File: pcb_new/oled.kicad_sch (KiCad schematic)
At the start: 33 parts, among them J10 3-2328724-1, U8 TPS6734ID

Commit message: initial test of new board
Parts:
- removed D1: SS12, OroLink:DIOM5027X244N, symbol OroLink:SS12
- added D1: SS12, OroLink:DIOM5027X244N, symbol SamacSys_Parts:SS12
- C105, C114, C115, C148: Mouser Part Number 81-GRM15C61E475ME15J -> (none)
- C89, C97: Mouser Part Number (none) -> 74-293D336X0020D2TE3; Mouser Price/Stock (none) -> https://www.mouser.de/ProductDetail/Vishay-Sprague/293D336X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
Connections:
- net +12V: now also D1.1
- net at L1.2, U8.6 (OUT): now also D1.2
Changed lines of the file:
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@@
 	)
 	(junction
-		(at 156.21 104.14)
-		(diameter 0)
-		(color 0 0 0 0)
-	)
-	(junction
 		(at 102.87 78.74)
 		(diameter 0)
@@
 	)
 	(junction
+		(at 156.21 104.14)
+		(diameter 0)
+		(color 0 0 0 0)
+	)
+	(junction
 		(at 243.84 120.65)
 		(diameter 0)
@@
 			)
 		)
-		(property "Mouser Part Number" "81-GRM15C61E475ME15J"
+		(property "Mouser Part Number" ""
 			(at 238.76 746.99 0)
 			(effects
@@
 	)
 	(symbol
-		(lib_id "OroLink:SS12")
-		(at 158.75 104.14 180)
-		(unit 1)
-		(exclude_from_sim no)
-		(in_bom yes)
-		(on_board yes)
-		(dnp no)
-		(fields_autoplaced yes)
-		(property "Reference" "D1"
-			(at 148.59 97.4555 0)
-			(effects
-				(font
-					(size 1.27 1.27)
-				)
-			)
-		)
-		(property "Value" "SS12"
-			(at 148.59 99.8798 0)
-			(effects
-				(font
-					(size 1.27 1.27)
-				)
-			)
-		)
-		(property "Footprint" "OroLink:DIOM5027X244N"
-			(at 146.05 10.49 0)
-			(effects
-				(font
-					(size 1.27 1.27)
-				)
-				(justify left top)
-				(hide yes)
-			)
-		)
-		(property "Datasheet" "https://www.panjit.com.tw/en/Product/downloadPDF/SS12"
-			(at 146.05 -89.51 0)
-			(effects
-				(font
-					(size 1.27 1.27)
-				)
-				(justify left top)
-				(hide yes)
-			)
-		)
-		(property "Description" "Power Schottky (IF1A) - SS12 , Standard, 20V, 1A, SMA"
-			(at 158.75 104.14 0)
-			(effects
-				(font
-					(size 1.27 1.27)
-				)
-				(hide yes)
-			)
-		)
-		(property "Height" "2.44"
-			(at 146.05 -289.51 0)
-			(effects
-				(font
-					(size 1.27 1.27)
-				)
-				(justify left top)
-				(hide yes)
-			)
-		)
-		(property "Manufacturer_Name" "PANJIT"
-			(at 146.05 -389.51 0)
-			(effects
-				(font
-					(size 1.27 1.27)
-				)
-				(justify left top)
-				(hide yes)
-			)
-		)
-		(property "Manufacturer_Part_Number" "SS12"
-			(at 146.05 -489.51 0)
-			(effects
-				(font
-					(size 1.27 1.27)
-				)
-				(justify left top)
-				(hide yes)
-			)
-		)
-		(property "Mouser Part Number" ""
-			(at 146.05 -589.51 0)
-			(effects
-				(font
-					(size 1.27 1.27)
-				)
-				(justify left top)
-				(hide yes)
-			)
-		)
-		(property "Mouser Price/Stock" ""
-			(at 146.05 -689.51 0)
-			(effects
-				(font
-					(size 1.27 1.27)
-				)
-				(justify left top)
-				(hide yes)
-			)
-		)
-		(property "Arrow Part Number" ""
-			(at 146.05 -789.51 0)
-			(effects
-				(font
-					(size 1.27 1.27)
-				)
-				(justify left top)
-				(hide yes)
-			)
-		)
-		(property "Arrow Price/Stock" ""
-			(at 146.05 -889.51 0)
-			(effects
-				(font
-					(size 1.27 1.27)
-				)
-				(justify left top)
-				(hide yes)
-			)
-		)
-		(pin "2"
-		)
-		(pin "1"
-		)
-		(instances
-			(project ""
-				(path "/b8dafc19-6de0-4c8f-9903-23372e5103df/222205f2-0600-4315-a593-542b8c55a37e"
-					(reference "D1")
-					(unit 1)
-				)
-			)
-		)
-	)
-	(symbol
 		(lib_id "OroLink:C1608X5R1H102K080AA")
 		(at 80.01 125.73 0)
@@
 	)
 	(symbol
+		(lib_name "293D336X0020D2TE3_1")
 		(lib_id "OroLink:293D336X0020D2TE3")
 		(at 118.11 99.06 0)
@@
 			)
 		)
-		(property "Mouser Part Number" ""
+		(property "Mouser Part Number" "74-293D336X0020D2TE3"
 			(at 127 795.25 0)
 			(effects
@@
 			)
 		)
-		(property "Mouser Price/Stock" ""
+		(property "Mouser Price/Stock" "https://www.mouser.de/ProductDetail/Vishay-Sprague/293D336X0020D2TE3?qs=CSo7yzBSerDt4rQKYL2h%252Bw%3D%3D"
 			(at 127 895.25 0)
 			(effects
@@
 			)
 		)
-		(property "Mouser Part Number" "81-GRM15C61E475ME15J"
+		(property "Mouser Part Number" ""
 			(at 210.82 807.95 0)
 			(effects
@@
 			)
 		)
-		(property "Mouser Part Number" "81-GRM15C61E475ME15J"
+		(property "Mouser Part Number" ""
 			(at 889.23 68.58 0)
 			(effects
@@
 	)
 	(symbol
+		(lib_id "SamacSys_Parts:SS12")
+		(at 158.75 104.14 180)
+		(unit 1)
+		(exclude_from_sim no)
+		(in_bom yes)
+		(on_board yes)
+		(dnp no)
+		(fields_autoplaced yes)
+		(property "Reference" "D1"
+			(at 148.59 97.9002 0)
+			(effects
+				(font
+					(size 1.27 1.27)
+				)
+			)
+		)
+		(property "Value" "SS12"
+			(at 148.59 100.4371 0)
+			(effects
+				(font
+					(size 1.27 1.27)
+				)
+			)
+		)
+		(property "Footprint" "OroLink:DIOM5027X244N"
+			(at 146.05 107.95 0)
+			(effects
+				(font
+					(size 1.27 1.27)
+				)
+				(justify left)
+				(hide yes)
+			)
+		)
+		(property "Datasheet" "https://datasheet.datasheetarchive.com/originals/distributors/Datasheets-24/DSA-463612.pdf"
+			(at 146.05 105.41 0)
+			(effects
+				(font
+					(size 1.27 1.27)
+				)
+				(justify left)
+				(hide yes)
+			)
+		)
+		(property "Description" "ON Semi SS12 SMT Schottky Diode, 20V 1A, 2-Pin DO-214AC"
+			(at 146.05 102.87 0)
+			(effects
+				(font
+					(size 1.27 1.27)
+				)
+				(justify left)
+				(hide yes)
+			)
+		)
+		(property "Height" "2.5"
+			(at 146.05 100.33 0)
+			(effects
+				(font
+					(size 1.27 1.27)
+				)
+				(justify left)
+				(hide yes)
+			)
+		)
+		(property "Manufacturer_Name" "onsemi"
+			(at 146.05 97.79 0)
+			(effects
+				(font
+					(size 1.27 1.27)
+				)
+				(justify left)
+				(hide yes)
+			)
+		)
+		(property "Manufacturer_Part_Number" "821-SS12"
+			(at 146.05 95.25 0)
+			(effects
+				(font
+					(size 1.27 1.27)
+				)
+				(justify left)
+				(hide yes)
+			)
+		)
+		(property "Mouser Part Number" "821-SS12"
+			(at 146.05 92.71 0)
+			(effects
+				(font
+					(size 1.27 1.27)
+				)
+				(justify left)
+				(hide yes)
+			)
+		)
+		(property "Mouser Price/Stock" "https://www.mouser.co.uk/ProductDetail/ON-Semiconductor-Fairchild/SS12?qs=mVVXn4M53U9WoaEpU1CO0A%3D%3D"
+			(at 146.05 90.17 0)
+			(effects
+				(font
+					(size 1.27 1.27)
+				)
+				(justify left)
+				(hide yes)
+			)
+		)
+		(property "Arrow Part Number" "SS12"
+			(at 146.05 87.63 0)
+			(effects
+				(font
+					(size 1.27 1.27)
+				)
+				(justify left)
+				(hide yes)
+			)
+		)
+		(property "Arrow Price/Stock" "https://www.arrow.com/en/products/ss12/on-semiconductor?region=nac"
+			(at 146.05 85.09 0)
+			(effects
+				(font
+					(size 1.27 1.27)
+				)
+				(justify left)
+				(hide yes)
+			)
+		)
+		(property "Mouser Testing Part Number" ""
+			(at 146.05 82.55 0)
+			(effects
+				(font
+					(size 1.27 1.27)
+				)
+				(justify left)
+				(hide yes)
+			)
+		)
+		(property "Mouser Testing Price/Stock" ""
+			(at 146.05 80.01 0)
+			(effects
+				(font
+					(size 1.27 1.27)
+				)
+				(justify left)
+				(hide yes)
+			)
+		)
+		(pin "1"
+		)
+		(pin "2"
+		)
+		(instances
+			(project "link"
+				(path "/b8dafc19-6de0-4c8f-9903-23372e5103df/222205f2-0600-4315-a593-542b8c55a37e"
+					(reference "D1")
+					(unit 1)
+				)
+			)
+		)
+	)
+	(symbol
 		(lib_id "OroLink:293D336X0020D2TE3")
 		(at 151.13 119.38 180)
@@
 			)
 		)
-		(property "Mouser Part Number" ""
+		(property "Mouser Part Number" "74-293D336X0020D2TE3"
 			(at 142.24 -576.81 0)
 			(effects
@@
 			)
 		)
-		(property "Mouser Price/Stock" ""
+		(property "Mouser Price/Stock" "https://www.mouser.de/ProductDetail/Vishay-Sprague/293D336X0020D2TE3?qs=CSo7yzBSerDt4rQKYL2h%252Bw%3D%3D"
 			(at 142.24 -676.81 0)
 			(effects
@@
 			)
 		)
-		(property "Mouser Part Number" "81-GRM15C61E475ME15J"
+		(property "Mouser Part Number" ""
 			(at 114.3 780.01 0)
 			(effects

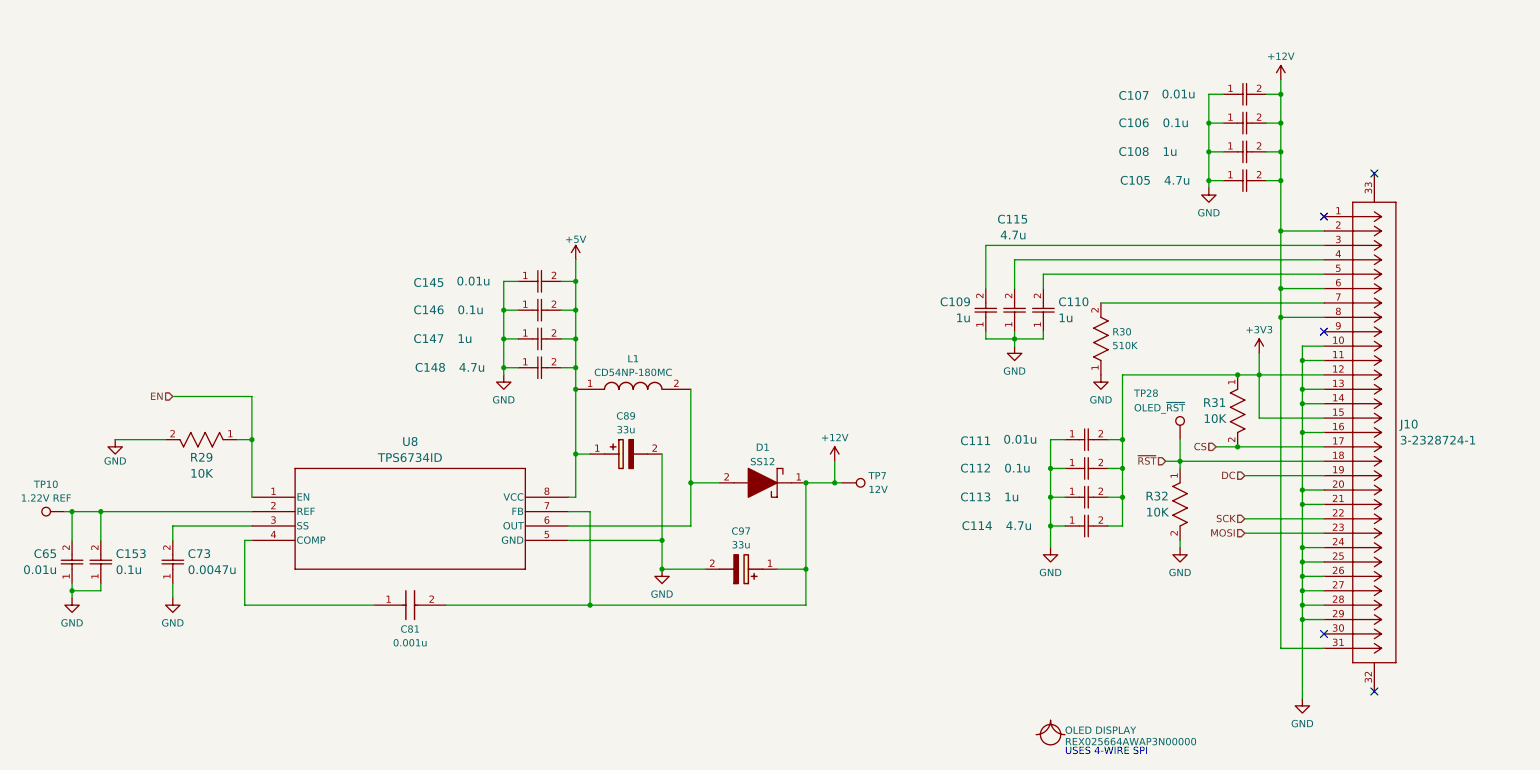
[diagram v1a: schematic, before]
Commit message: fix OLED port wiring (ref #63)
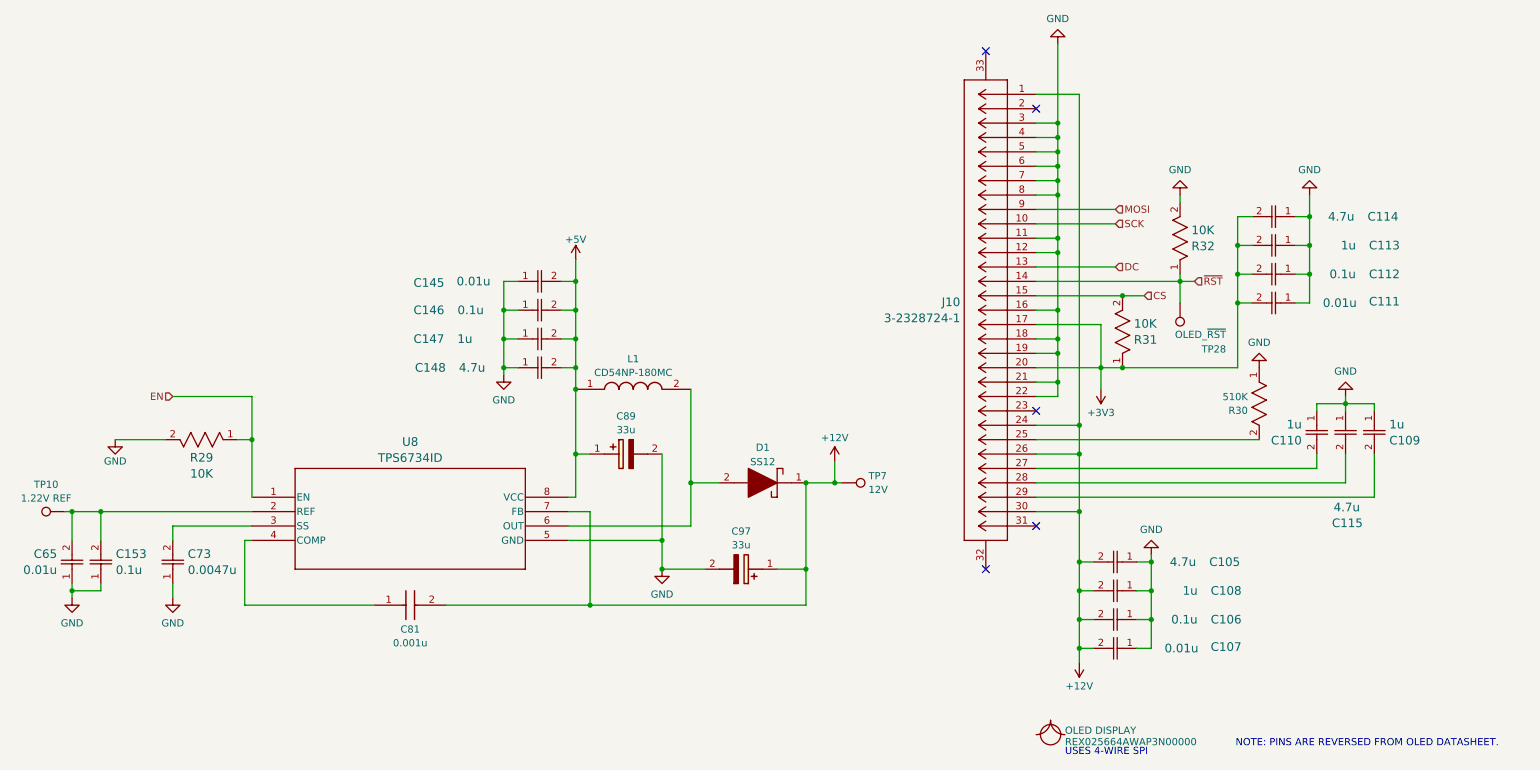
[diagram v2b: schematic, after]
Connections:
- net +12V: now also J10.1, J10.24, J10.26, J10.30; no longer J10.2, J10.31, J10.6, J10.8
- net +3V3: now also J10.17, J10.20; no longer J10.12, J10.15
- net CS: now also J10.15; no longer J10.17
- net DC: now also J10.13; no longer J10.19
- net GND: now also J10.12, J10.18, J10.19, J10.22, J10.3, J10.4, J10.5, J10.6, J10.7, J10.8; no longer J10.10, J10.13, J10.14, J10.20, J10.24, J10.25, J10.26, J10.27, J10.28, J10.29
- net MOSI: now also J10.9; no longer J10.23
- net SCK: now also J10.10; no longer J10.22
- net ~{RST}: now also J10.14; no longer J10.18
- net at C110.2: now also J10.27; no longer J10.5
- net at C109.2: now also J10.29; no longer J10.3
- net at C115.2: now also J10.28; no longer J10.4
- net at R30.2: now also J10.25; no longer J10.7
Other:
- note added: "NOTE: PINS ARE REVERSED FROM OLED DATASHEET."
- moved on the sheet: C105, C106, C107, C108, C109, C110, C111, C112, C113, C114, C115, J10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

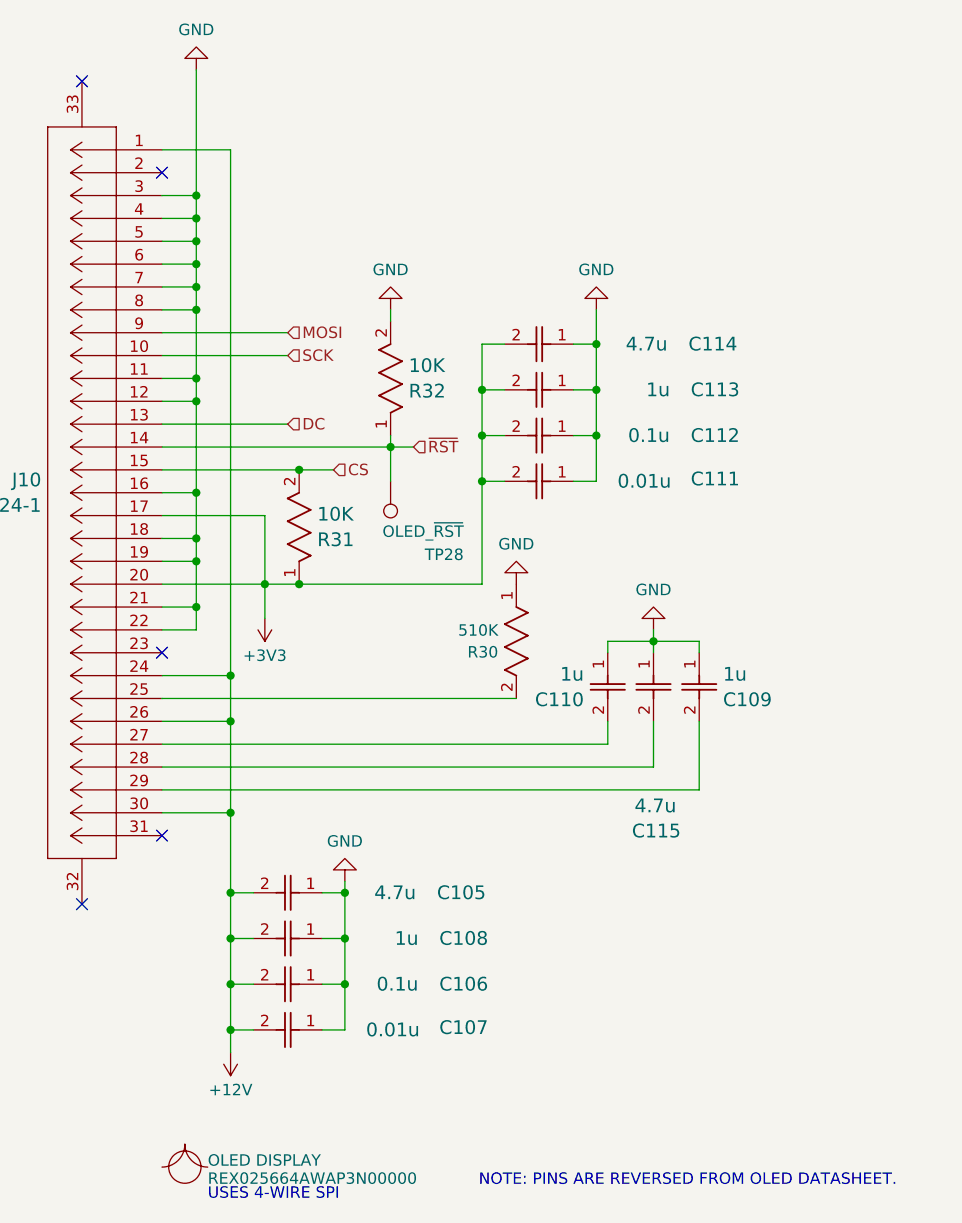
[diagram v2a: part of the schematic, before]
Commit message: re-format OLED (ref #63), pull down DC (ref #70) and remove RST TP (closes #93)
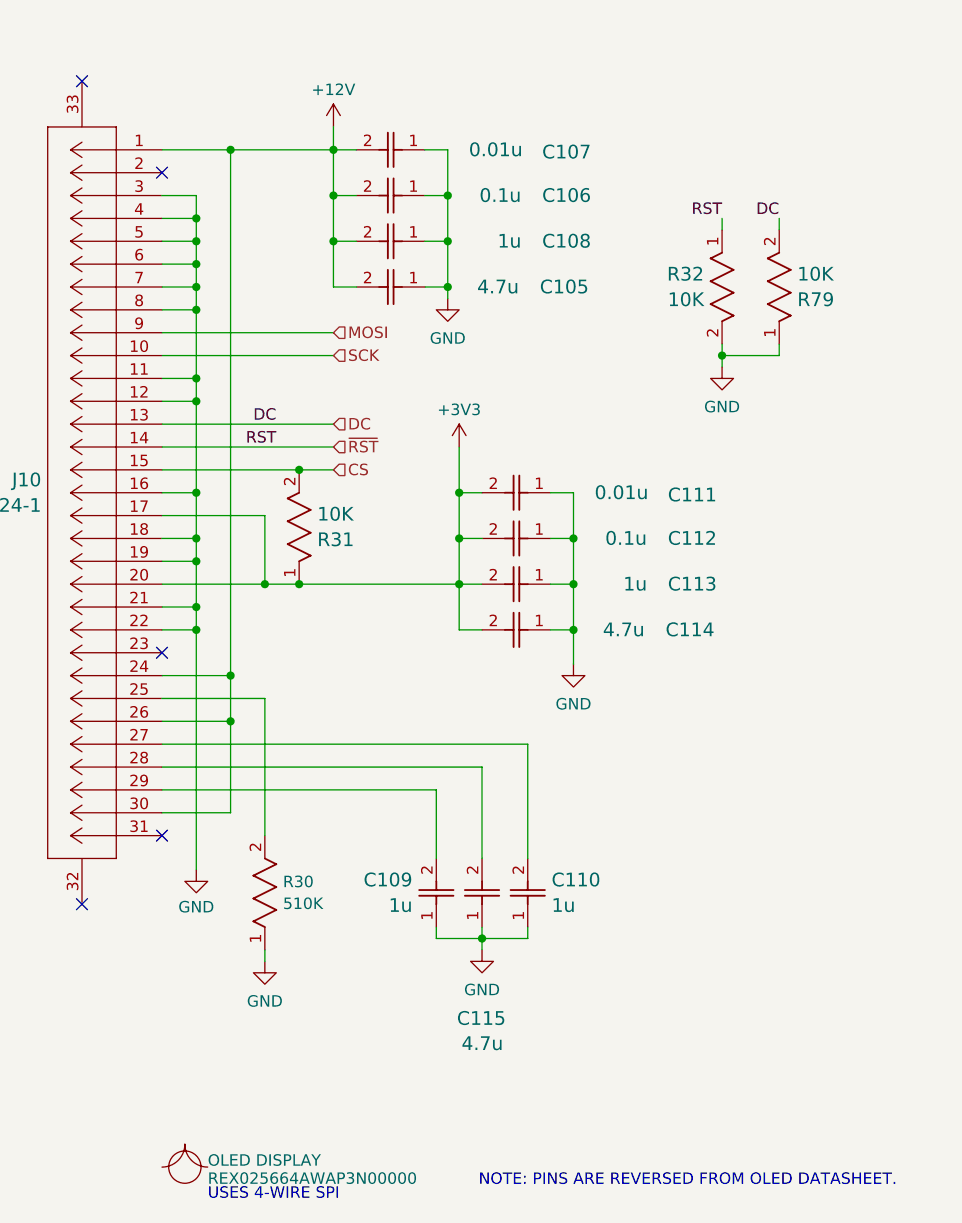
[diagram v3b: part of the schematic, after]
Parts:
- removed TP28: OLED_~{RST}, TestPoint:TestPoint_Pad_1.0x1.0mm, symbol Connector:TestPoint
- added R79: 10K, OroLink:STA_RMCF0402_STP, symbol OroLink:RMCF0402FT10K0
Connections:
- net DC: now also R79.2
- net GND: now also R79.1
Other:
- moved on the sheet: C105, C106, C107, C108, C109, C110, C111, C112, C113, C114, C115, R30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

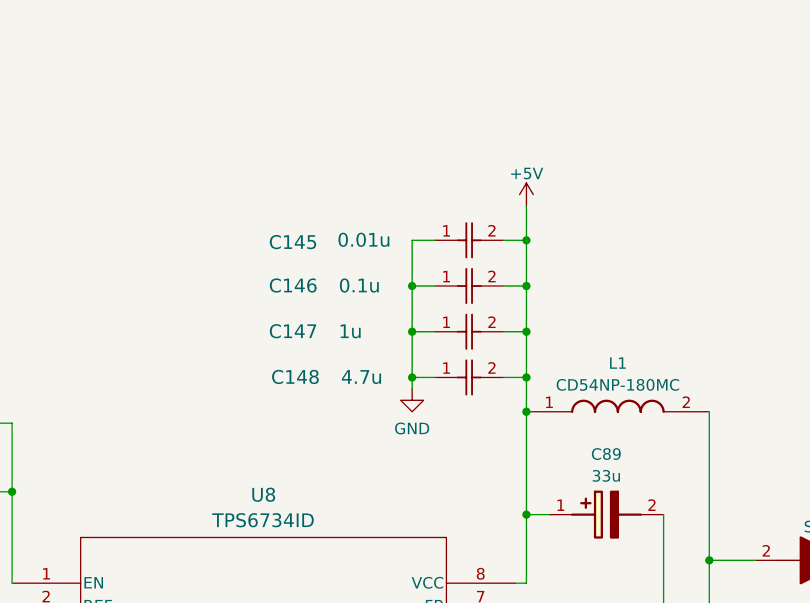
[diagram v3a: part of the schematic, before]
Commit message: remove additional 12V VIN bypass caps (closes #94)
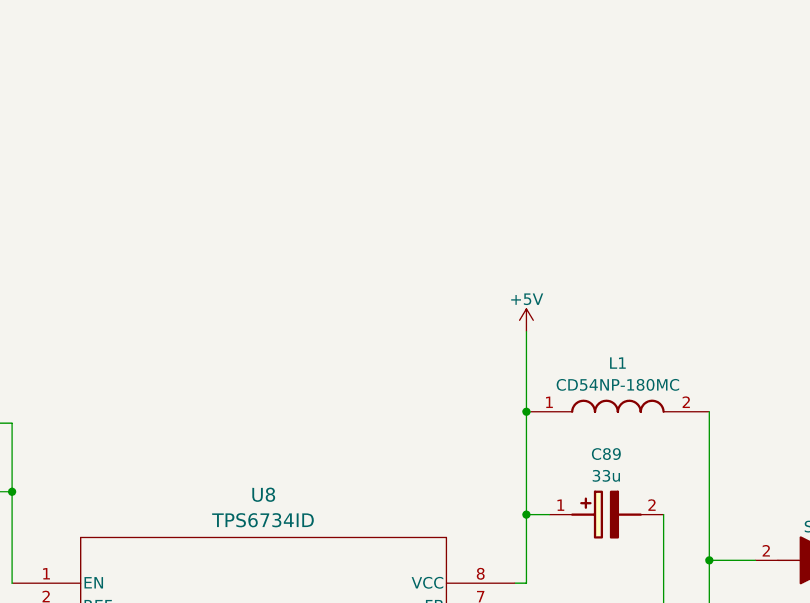
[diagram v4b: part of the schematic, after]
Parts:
- removed C145: 0.01u, OroLink:CAP_0402_N_WAL, symbol OroLink:0402B103J160CT
- removed C146: 0.1u, OroLink:CAP_MSAS1L-3_TAY, symbol OroLink:MSAST1L3YB5104KFNA01
- removed C147: 1u, OroLink:cap_UMK105 CG080CV-F_TAY, symbol OroLink:JMK105BJ105KVHF
- removed C148: 4.7u, OroLink:GRM15x, symbol OroLink:GRM155C61E475ME15J
